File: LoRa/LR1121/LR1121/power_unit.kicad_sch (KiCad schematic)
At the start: 24 parts, among them J3 ConnBattery, U7 BQ25619ERTWR

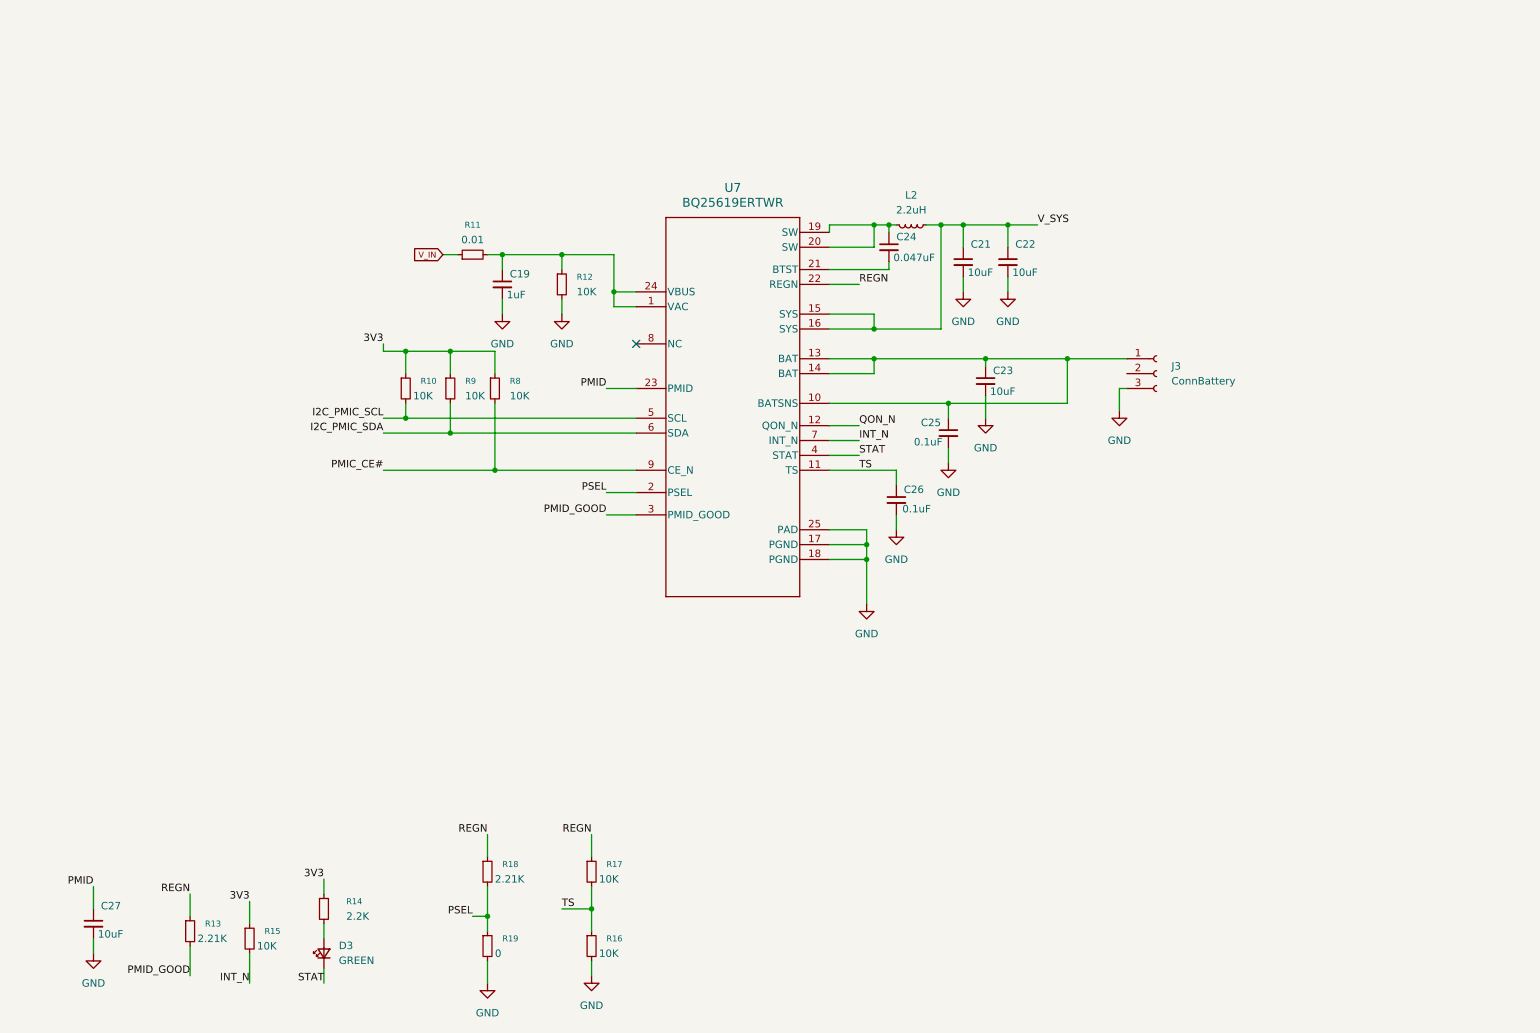
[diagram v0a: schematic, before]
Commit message: [IMX8ML] Add new layer
A new layers was add in the cpu schematic, now it had 8 layer.
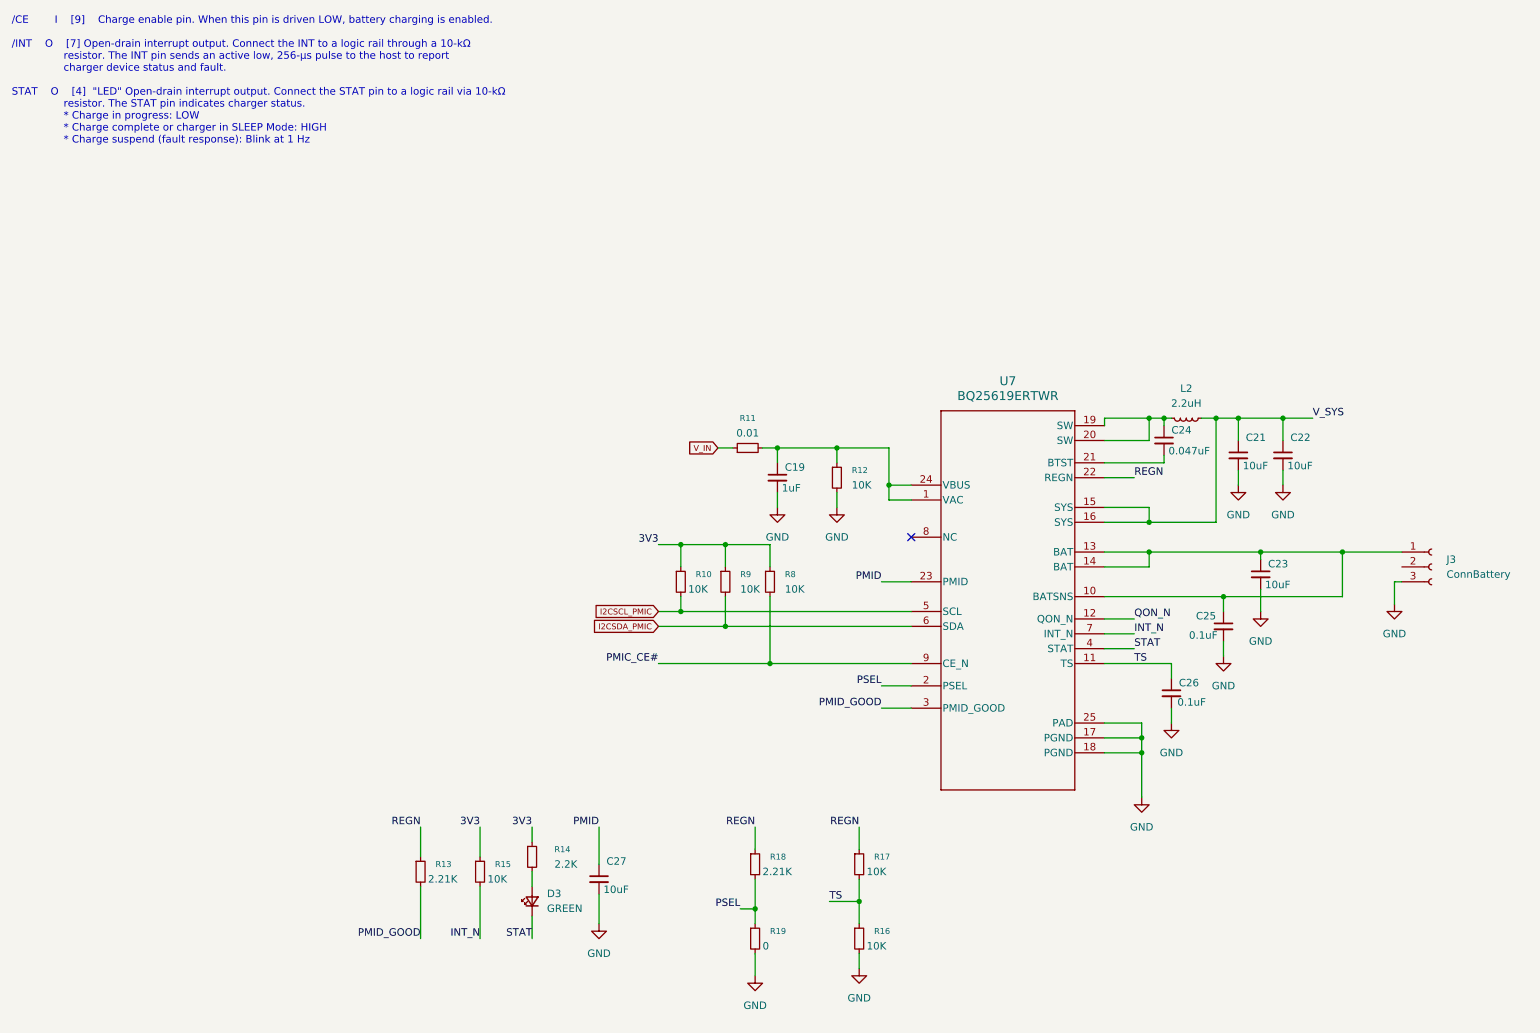
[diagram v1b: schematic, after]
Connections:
- net I2C_PMIC_SCL renamed I2CSCL_PMIC
- net I2C_PMIC_SDA renamed I2CSDA_PMIC
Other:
- note added: "/CE I [9] Charge enable pin. When this pin is driven LOW, battery charging is enabled. /INT O [7] Open-drain interrupt output. Connect the INT to a logic rail through a 10-kΩ resistor. The INT pin sends an active low, 256-µs pulse to the host to report charger device status and fault. STAT O [4] "LED" Open-drain interrupt output. Connect the STAT pin to a logic rail via 10-kΩ resistor. The STAT p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"
- moved on the sheet: C19, C21, C22, C23, C24, C25, C26, C27, D3, J3, L2, R10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
